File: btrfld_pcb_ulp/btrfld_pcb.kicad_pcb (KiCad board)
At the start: 2 copper layers, 82 x 64.8 mm, 41 parts

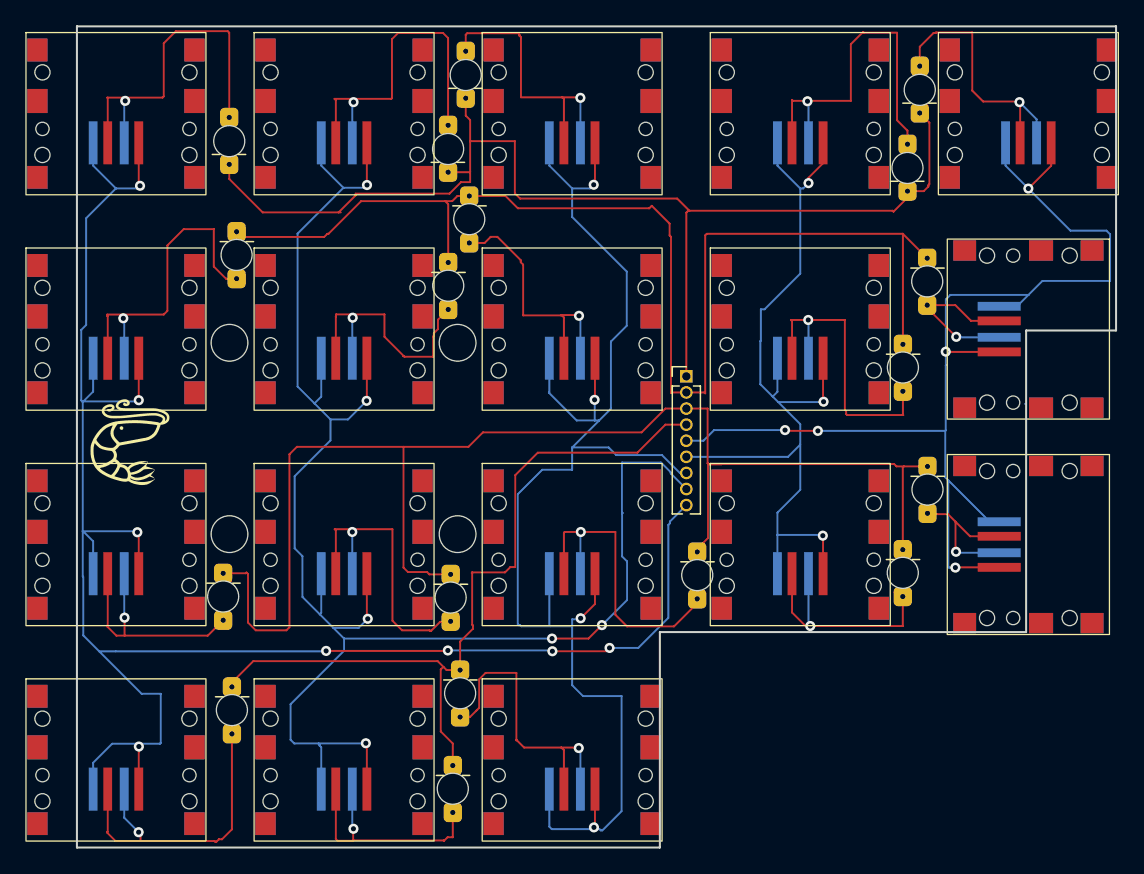
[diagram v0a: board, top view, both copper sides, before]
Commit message: place and test body pcb and cad screw holes
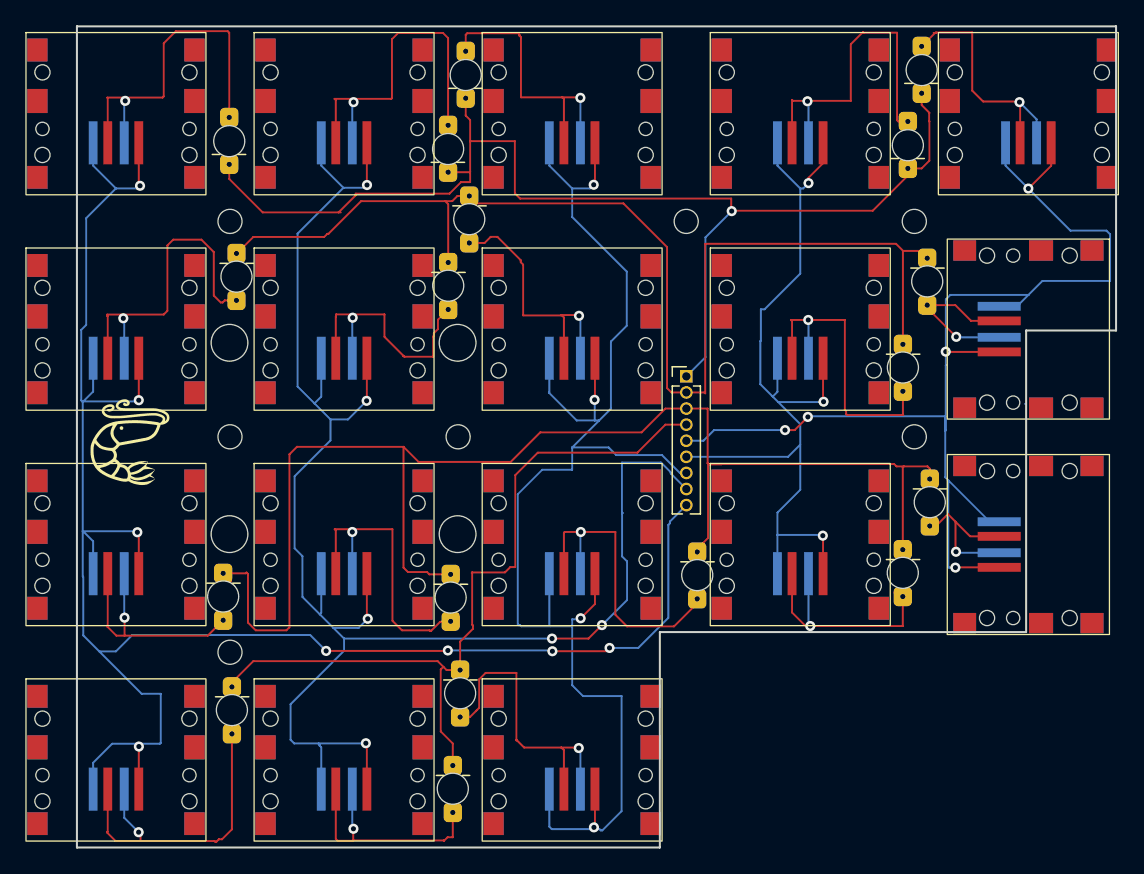
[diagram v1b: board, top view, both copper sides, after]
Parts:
- added ?: , , F.Cu at (108.3, 70.8)
- added ?: , , F.Cu at (162.3, 70.8)
- added ?: , , F.Cu at (108.3, 104.8)
- added ?: , , F.Cu at (108.3, 87.8)
- added ?: , , F.Cu at (162.3, 87.8)
- added ?: , , F.Cu at (144.3, 70.8)
- added ?: , , B.Cu at (126.3, 87.8)
- moved REF** 1.79 mm to (161.8, 67.9)
- moved REF** 1.71 mm to (108.8, 72.2)
- moved REF** 1.57 mm to (162.9, 61.9)
- moved REF** 1.01 mm to (163.5, 90.0)
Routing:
- net (no net): track 1335.9 -> 1337.1 mm, vias 44 -> 45
